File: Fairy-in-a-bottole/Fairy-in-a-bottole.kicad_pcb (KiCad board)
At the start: 2 copper layers, 6 parts, among them J1 FTDI, U1 ESP32-WROOM-32D, U2 AMS1117-3.3

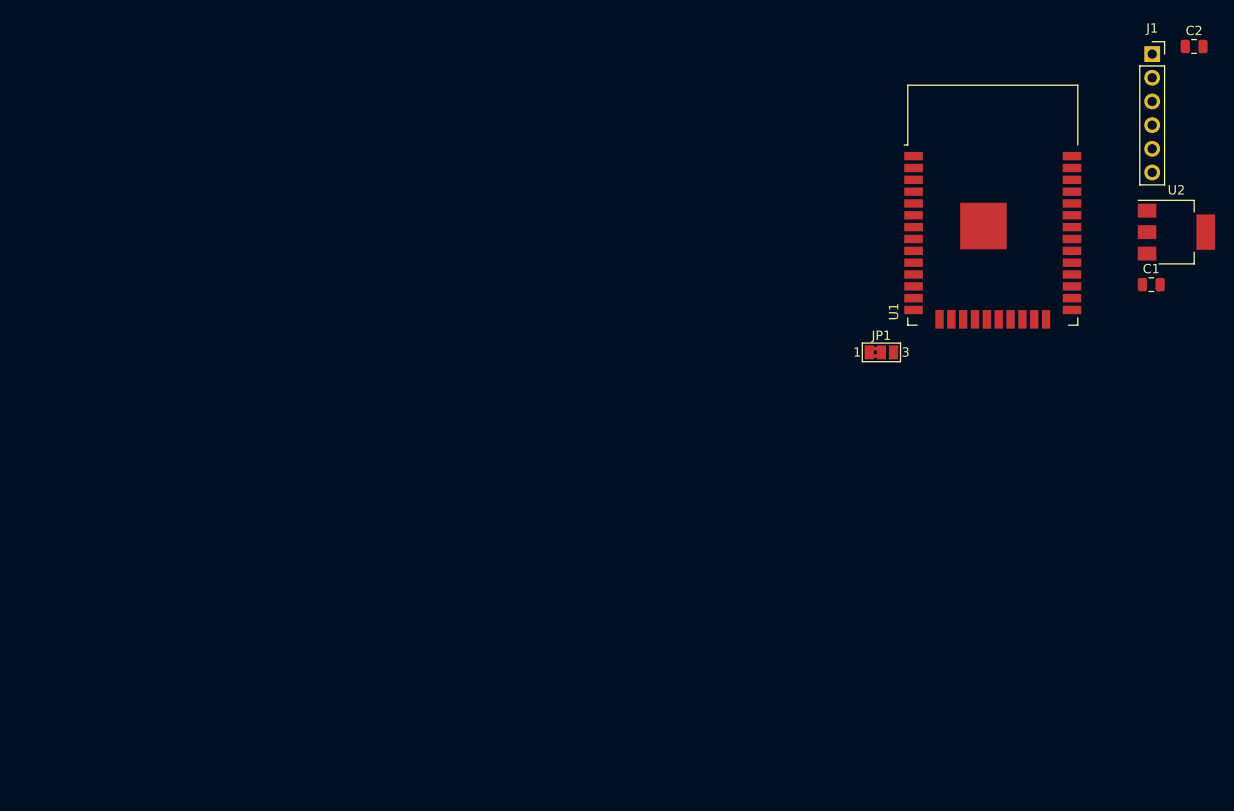
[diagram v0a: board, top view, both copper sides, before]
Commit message: asigned foorprints and populated the pcb with them
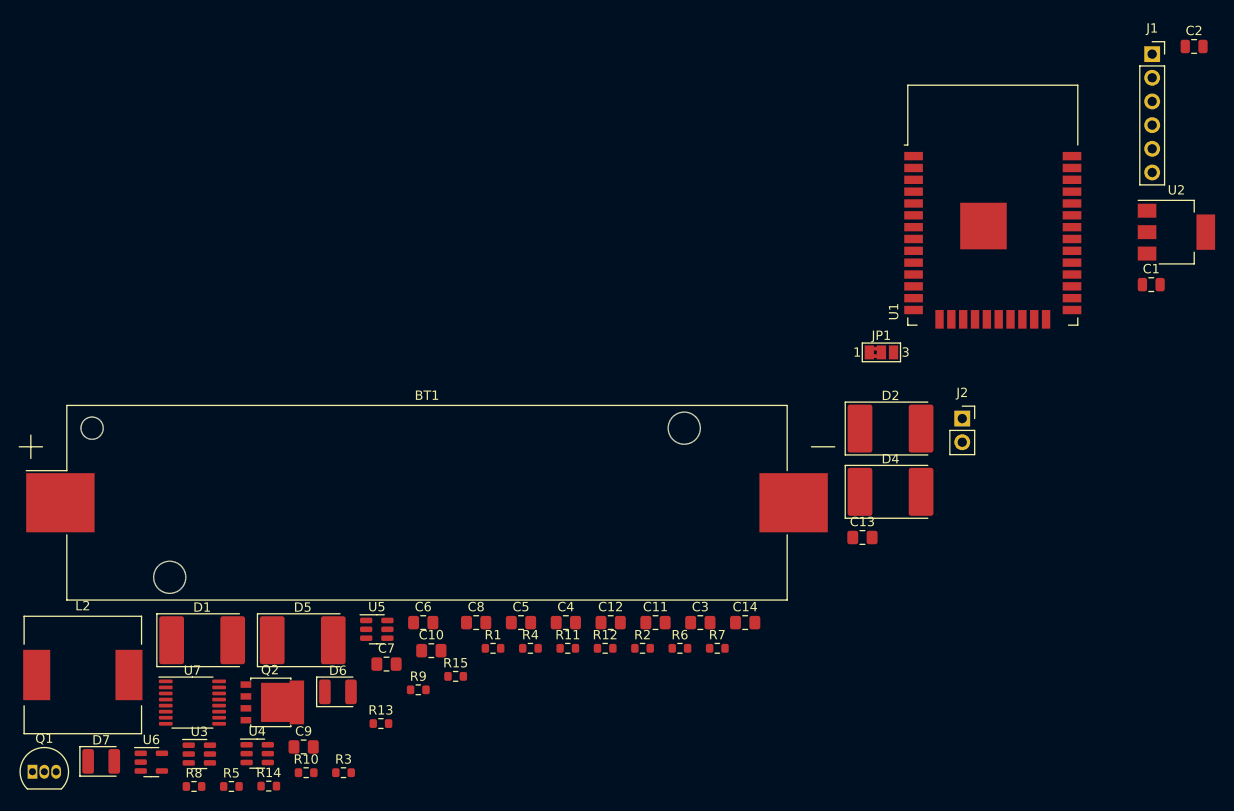
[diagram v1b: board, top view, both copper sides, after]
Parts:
- added BT1: Battery_Cell, Battery:BatteryHolder_Keystone_1042_1x18650, F.Cu at (83.7, 112.5)
- added C10: C, Capacitor_SMD:C_0805_2012Metric_Pad1.18x1.45mm_HandSolder, F.Cu at (84.2, 128.4)
- added C11: C, Capacitor_SMD:C_0805_2012Metric_Pad1.18x1.45mm_HandSolder, F.Cu at (108.2, 125.4)
- added C12: C, Capacitor_SMD:C_0805_2012Metric_Pad1.18x1.45mm_HandSolder, F.Cu at (103.4, 125.4)
- added C13: C, Capacitor_SMD:C_0805_2012Metric_Pad1.18x1.45mm_HandSolder, F.Cu at (130.4, 116.2)
- added C14: C, Capacitor_SMD:C_0805_2012Metric_Pad1.18x1.45mm_HandSolder, F.Cu at (117.8, 125.4)
- added C3: C, Capacitor_SMD:C_0805_2012Metric_Pad1.18x1.45mm_HandSolder, F.Cu at (113.0, 125.4)
- added C4: C, Capacitor_SMD:C_0805_2012Metric_Pad1.18x1.45mm_HandSolder, F.Cu at (98.6, 125.4)
- added C5: C, Capacitor_SMD:C_0805_2012Metric_Pad1.18x1.45mm_HandSolder, F.Cu at (93.8, 125.4)
- added C6: C, Capacitor_SMD:C_0805_2012Metric_Pad1.18x1.45mm_HandSolder, F.Cu at (83.3, 125.4)
- added C7: C, Capacitor_SMD:C_0805_2012Metric_Pad1.18x1.45mm_HandSolder, F.Cu at (79.4, 129.8)
- added C8: C, Capacitor_SMD:C_0805_2012Metric_Pad1.18x1.45mm_HandSolder, F.Cu at (89.0, 125.4)
- added C9: C, Capacitor_SMD:C_0805_2012Metric_Pad1.18x1.45mm_HandSolder, F.Cu at (70.5, 138.7)
- added D1: LED, Diode_SMD:D_3220_8050Metric_Pad2.65x5.15mm_HandSolder, F.Cu at (59.6, 127.2)
- added D2: LED, Diode_SMD:D_3220_8050Metric_Pad2.65x5.15mm_HandSolder, F.Cu at (133.4, 104.5)
- added D4: LED, Diode_SMD:D_3220_8050Metric_Pad2.65x5.15mm_HandSolder, F.Cu at (133.4, 111.3)
- added D5: LED, Diode_SMD:D_3220_8050Metric_Pad2.65x5.15mm_HandSolder, F.Cu at (70.4, 127.2)
- added D6: D_Zener, Diode_SMD:D_1210_3225Metric, F.Cu at (74.1, 132.8)
- added D7: D_Zener, Diode_SMD:D_1210_3225Metric, F.Cu at (48.7, 140.2)
- added J2: Solar/PWR in, Connector_PinSocket_2.54mm:PinSocket_1x02_P2.54mm_Vertical, F.Cu at (141.1, 103.5)
- added L2: L, Inductor_SMD:L_12x12mm_H8mm, F.Cu at (46.8, 131.0)
- added Q1: 2N7000, Package_TO_SOT_THT:TO-92_Inline, F.Cu at (41.4, 141.4)
- added Q2: PSMN5R2-60YL, Package_TO_SOT_SMD:LFPAK56, F.Cu at (67.1, 133.9)
- added R1: R, Resistor_SMD:R_0603_1608Metric, F.Cu at (90.8, 128.1)
- added R10: R, Resistor_SMD:R_0603_1608Metric, F.Cu at (70.7, 141.5)
- added R11: R, Resistor_SMD:R_0603_1608Metric, F.Cu at (98.8, 128.1)
- added R12: R, Resistor_SMD:R_0603_1608Metric, F.Cu at (102.8, 128.1)
- added R13: R, Resistor_SMD:R_0603_1608Metric, F.Cu at (78.8, 136.2)
- added R14: R, Resistor_SMD:R_0603_1608Metric, F.Cu at (66.7, 142.9)
- added R15: R, Resistor_SMD:R_0603_1608Metric, F.Cu at (86.8, 131.1)
- added R2: R, Resistor_SMD:R_0603_1608Metric, F.Cu at (106.8, 128.1)
- added R3: R, Resistor_SMD:R_0603_1608Metric, F.Cu at (74.7, 141.5)
- added R4: R, Resistor_SMD:R_0603_1608Metric, F.Cu at (94.8, 128.1)
- added R5: 100r, Resistor_SMD:R_0603_1608Metric, F.Cu at (62.7, 142.9)
- added R6: R, Resistor_SMD:R_0603_1608Metric, F.Cu at (110.8, 128.1)
- added R7: R, Resistor_SMD:R_0603_1608Metric, F.Cu at (114.8, 128.1)
- added R8: R, Resistor_SMD:R_0603_1608Metric, F.Cu at (58.7, 142.9)
- added R9: R, Resistor_SMD:R_0603_1608Metric, F.Cu at (82.8, 132.6)
- added U3: BL8573CB6TR, Package_TO_SOT_SMD:SOT-23-6, F.Cu at (59.3, 139.5)
- added U4: FS8205A, Package_TO_SOT_SMD:SOT-23-6, F.Cu at (65.5, 139.4)
- added U5: DW01A, Package_TO_SOT_SMD:SOT-23-6, F.Cu at (78.3, 126.1)
- added U6: SLM2169, Package_TO_SOT_SMD:SOT-23-5, F.Cu at (54.1, 140.3)
- added U7: CN3722, Package_SO:TSSOP-16_4.4x5mm_P0.65mm, F.Cu at (58.5, 133.9)
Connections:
- net Net-(C1-Pad1) renamed +5V
